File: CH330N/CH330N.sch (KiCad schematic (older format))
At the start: 19 parts, among them J2 Conn_01x06, P1 USB_C_Plug_USB2.0, U1 CH330N, U2 AP2127K-3.3

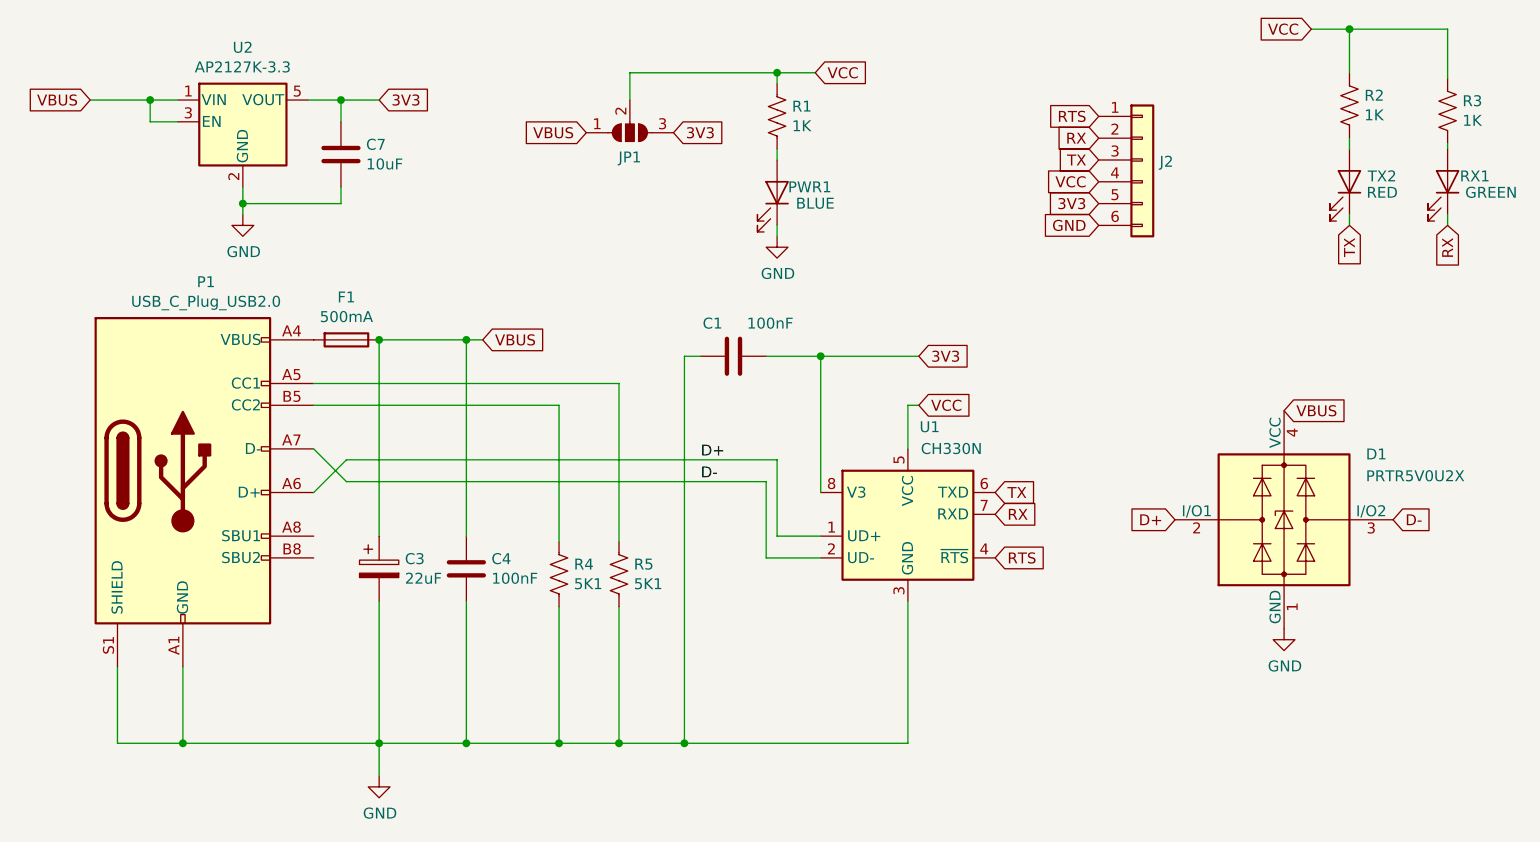
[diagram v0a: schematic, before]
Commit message: SirUSB Board Revisions
Removed MicroUSB Versions of FT230 and FT231, SolderPaste Layer Adjusted to -0.05mm, Silkscreens optimised, OSHW logo added.
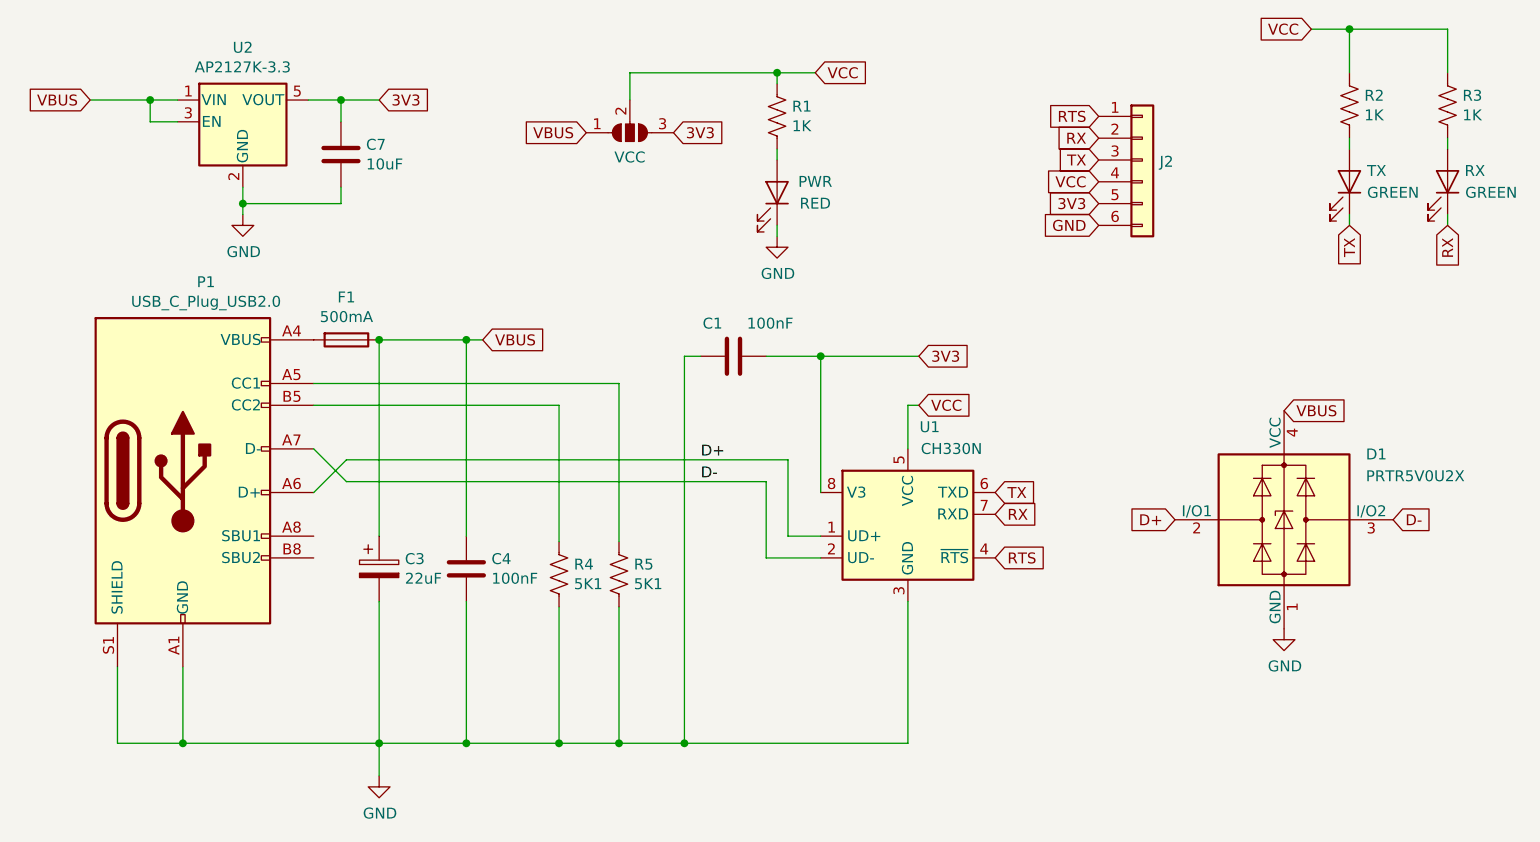
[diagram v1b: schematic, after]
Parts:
- PWR: renamed from PWR1; value BLUE -> RED; Part C193191 -> C118330
- TX: renamed from TX2; value RED -> GREEN; Part C118330 -> C205443
- renumbered RX1 to RX, JP1 to VCC
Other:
- moved on the sheet: R3
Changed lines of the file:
@@
 	4775 3250 4775 3900
 Wire Wire Line
-	4375 2950 4175 2950
-Wire Wire Line
-	4175 2950 4175 2600
+	4375 2950 4225 2950
+Wire Wire Line
+	4225 2950 4225 2600
 Wire Wire Line
 	4125 2700 4125 3050
@@
 	2200 2600 2050 2750
 Wire Wire Line
-	2200 2600 4175 2600
+	2200 2600 4225 2600
 Wire Wire Line
 	2200 2700 2050 2550
@@
 $EndComp
 $Comp
-L Jumper:SolderJumper_3_Open JP1
+L Jumper:SolderJumper_3_Open VCC
 U 1 1 5D65075B
 P 3500 1100
-F 0 "JP1" H 3500 1213 50  0000 C CNN
+F 0 "VCC" H 3500 1213 50  0000 C CNN
 F 1 "SolderJumper_3_Open" H 3500 1213 50  0001 C CNN
 F 2 "Jumper:SolderJumper-3_P1.3mm_Open_RoundedPad1.0x1.5mm" H 3500 1100 50  0001 C CNN
@@
 	3500 825  4175 825
 Wire Wire Line
-	7250 1175 7250 1150
-Wire Wire Line
 	7250 1525 7250 1475
-$Comp
-L Device:R_US R3
-U 1 1 5E4C8EDB
-P 7250 1000
-F 0 "R3" H 7318 1045 50  0000 L CNN
-F 1 "1K" H 7318 955 50  0000 L CNN
-F 2 "Resistor_SMD:R_0603_1608Metric" V 7290 990 50  0001 C CNN
-F 3 "~" H 7250 1000 50  0001 C CNN
-F 4 "C25585" H 7250 1000 50  0001 C CNN "Part"
-	1    7250 1000
-	1    0    0    -1
-$EndComp
 Text GLabel 7250 1525 3    50   Input ~ 0
 RX
 Text GLabel 6800 1525 3    50   Input ~ 0
 TX
-$Comp
-L Device:LED RX1
-U 1 1 5E4CEE4C
-P 7250 1325
-F 0 "RX1" V 7275 1450 50  0000 C CNN
-F 1 "GREEN" V 7200 1525 50  0000 C CNN
-F 2 "LED_SMD:LED_0603_1608Metric" H 7250 1325 50  0001 C CNN
-F 3 "~" H 7250 1325 50  0001 C CNN
-F 4 "C205443" H 7250 1325 50  0001 C CNN "Part"
-	1    7250 1325
-	0    1    -1   0
-$EndComp
 Wire Wire Line
 	6800 1525 6800 1475
@@
 	1    0    0    -1
 $EndComp
-$Comp
-L Device:LED TX2
-U 1 1 5E4E74BC
-P 6800 1325
-F 0 "TX2" V 6825 1475 50  0000 C CNN
-F 1 "RED" V 6750 1475 50  0000 C CNN
-F 2 "LED_SMD:LED_0603_1608Metric" H 6800 1325 50  0001 C CNN
-F 3 "~" H 6800 1325 50  0001 C CNN
-F 4 "C118330" H 6800 1325 50  0001 C CNN "Part"
-	1    6800 1325
-	0    1    -1   0
-$EndComp
 Wire Wire Line
 	4175 1575 4175 1525
@@
 	1    4175 1025
 	1    0    0    -1
-$EndComp
-$Comp
-L Device:LED PWR1
-U 1 1 5E4F8641
-P 4175 1375
-F 0 "PWR1" V 4200 1525 50  0000 C CNN
-F 1 "BLUE" V 4125 1550 50  0000 C CNN
-F 2 "LED_SMD:LED_0603_1608Metric" H 4175 1375 50  0001 C CNN
-F 3 "~" H 4175 1375 50  0001 C CNN
-F 4 "C193191" H 4175 1375 50  0001 C CNN "Part"
-	1    4175 1375
-	0    1    -1   0
 $EndComp
 Connection ~ 4175 825
@@
 VCC
 Wire Wire Line
-	7250 850  7250 625
-Wire Wire Line
 	6625 625  6800 625
 Wire Wire Line
@@
 Wire Wire Line
 	1025 950  1300 950
+$Comp
+L Device:LED RX
+U 1 1 5E4CEE4C
+P 7250 1325
+F 0 "RX" V 7300 1450 50  0000 C CNN
+F 1 "GREEN" V 7200 1525 50  0000 C CNN
+F 2 "LED_SMD:LED_0603_1608Metric" H 7250 1325 50  0001 C CNN
+F 3 "~" H 7250 1325 50  0001 C CNN
+F 4 "C205443" H 7250 1325 50  0001 C CNN "Part"
+	1    7250 1325
+	0    1    -1   0
+$EndComp
+$Comp
+L Device:LED TX
+U 1 1 5E4E74BC
+P 6800 1325
+F 0 "TX" V 6850 1450 50  0000 C CNN
+F 1 "GREEN" V 6750 1525 50  0000 C CNN
+F 2 "LED_SMD:LED_0603_1608Metric" H 6800 1325 50  0001 C CNN
+F 3 "~" H 6800 1325 50  0001 C CNN
+F 4 "C205443" H 6800 1325 50  0001 C CNN "Part"
+	1    6800 1325
+	0    1    -1   0
+$EndComp
+$Comp
+L Device:R_US R3
+U 1 1 5E4C8EDB
+P 7250 975
+F 0 "R3" H 7318 1020 50  0000 L CNN
+F 1 "1K" H 7318 930 50  0000 L CNN
+F 2 "Resistor_SMD:R_0603_1608Metric" V 7290 965 50  0001 C CNN
+F 3 "~" H 7250 975 50  0001 C CNN
+F 4 "C25585" H 7250 975 50  0001 C CNN "Part"
+	1    7250 975
+	1    0    0    -1
+$EndComp
+Wire Wire Line
+	7250 825  7250 625
+Wire Wire Line
+	7250 1175 7250 1125
+$Comp
+L Device:LED PWR
+U 1 1 5E4F8641
+P 4175 1375
+F 0 "PWR" V 4225 1550 50  0000 C CNN
+F 1 "RED" V 4125 1550 50  0000 C CNN
+F 2 "LED_SMD:LED_0603_1608Metric" H 4175 1375 50  0001 C CNN
+F 3 "~" H 4175 1375 50  0001 C CNN
+F 4 "C118330" H 4175 1375 50  0001 C CNN "Part"
+	1    4175 1375
+	0    1    -1   0
+$EndComp
 $EndSCHEMATC
